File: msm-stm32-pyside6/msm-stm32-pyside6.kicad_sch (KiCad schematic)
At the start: 18 parts, among them U1 L3GD20, U2 STM32L476VGTx

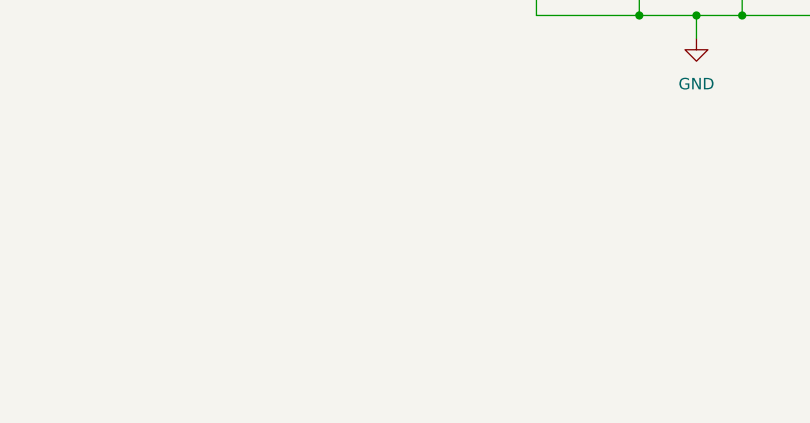
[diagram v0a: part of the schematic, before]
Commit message: Use shared symbol library, draw a bit of GPIO input stage
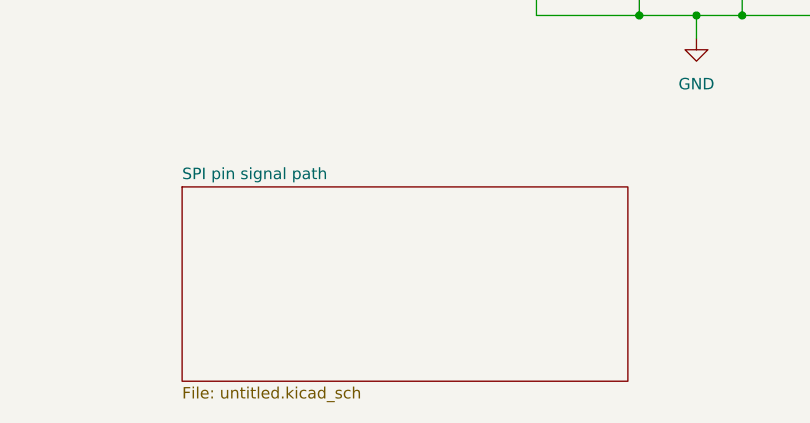
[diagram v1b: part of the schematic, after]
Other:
- added sheet SPI pin signal path (untitled.kicad_sch)
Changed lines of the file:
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@@
+		)
+	)
+	(sheet
+		(at 120.65 162.56)
+		(size 49.53 21.59)
+		(exclude_from_sim yes)
+		(in_bom no)
+		(on_board no)
+		(dnp no)
+		(fields_autoplaced yes)
+		(stroke
+			(width 0.1524)
+			(type solid)
+		)
+		(fill
+			(color 0 0 0 0.0000)
+		)
+		(property "Sheetname" "SPI pin signal path"
+			(at 120.65 161.8484 0)
+			(effects
+				(font
+					(size 1.27 1.27)
+				)
+				(justify left bottom)
+			)
+		)
+		(property "Sheetfile" "untitled.kicad_sch"
+			(at 120.65 184.7346 0)
+			(effects
+				(font
+					(size 1.27 1.27)
+				)
+				(justify left top)
+			)
+		)
+		(instances
+			(project "msm-stm32-pyside6"
+				(path "/f9c1f6c8-5521-4ac3-8af7-7ae3643e916d"
+					(page "2")
+				)
+			)
 		)
 	)
